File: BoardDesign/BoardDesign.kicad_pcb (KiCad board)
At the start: 2 copper layers, 77.5 x 67.3 mm, 10 parts

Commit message: Fixed Issue with R4 Trace
Had an accidental junction in the schematic.
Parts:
- renumbered 330 to R1, 10k to R5, Screen to U1, 74HC595 to U2
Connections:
- A1 pad 7: Net-(A1-Pad16) -> Net-(A1-Pad7)
- R1 pad 2: Net-(A1-Pad16) -> Net-(A1-Pad7)
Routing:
- net Net-(A1-Pad16): track 33.3 -> 57.5 mm, vias 0 -> 2
- net Net-(A1-Pad7): track 0.00 -> 6.68 mm

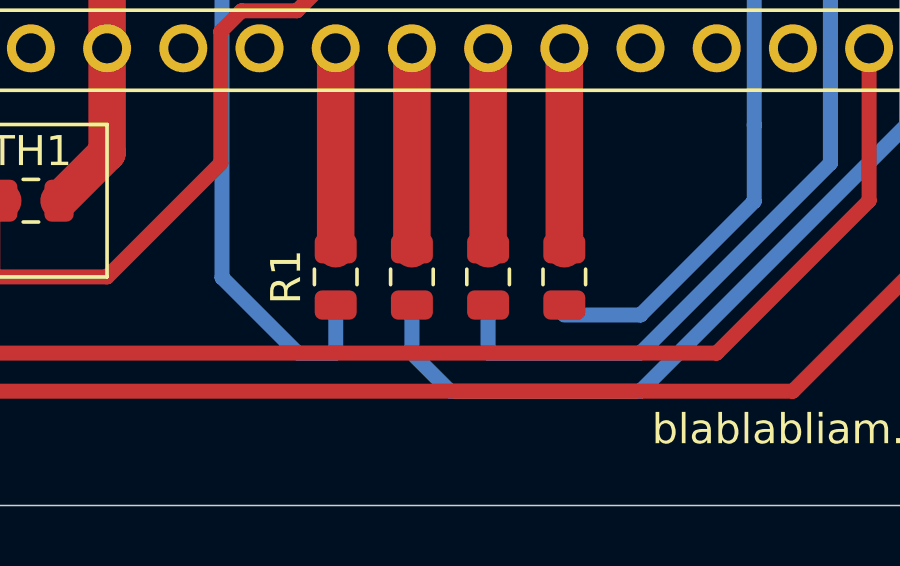
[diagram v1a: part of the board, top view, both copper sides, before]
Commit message: Fixed issue with 330 R trace on wrong side of board
The 330 ohm resistors have the traces on the wrong side of the board, so
that the resistors are not actually connected to anything. Fixed with 4
vias.
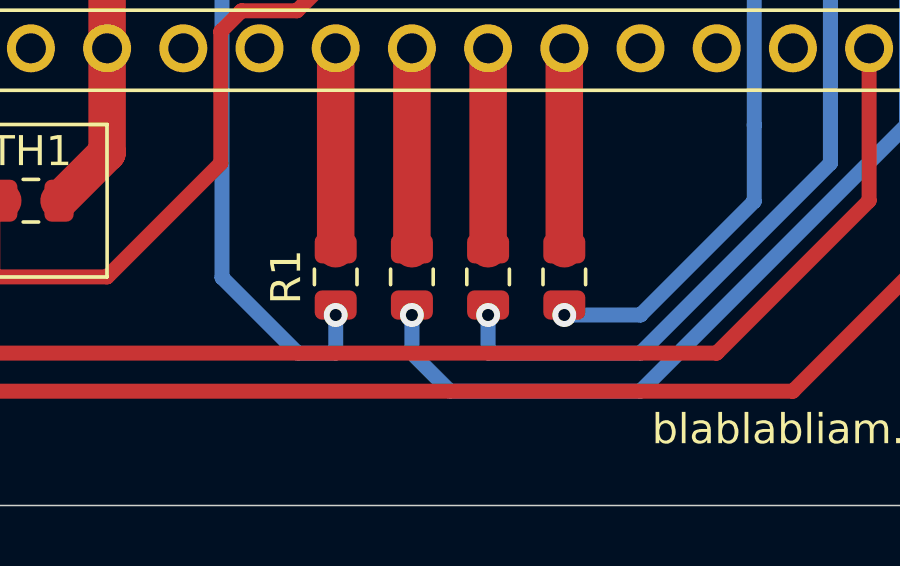
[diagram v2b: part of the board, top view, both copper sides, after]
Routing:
- net Net-(R4-Pad1): vias 0 -> 1
- net Net-(R3-Pad1): vias 0 -> 1
- net Net-(R2-Pad2): vias 0 -> 1
- net Net-(R1-Pad1): vias 0 -> 1

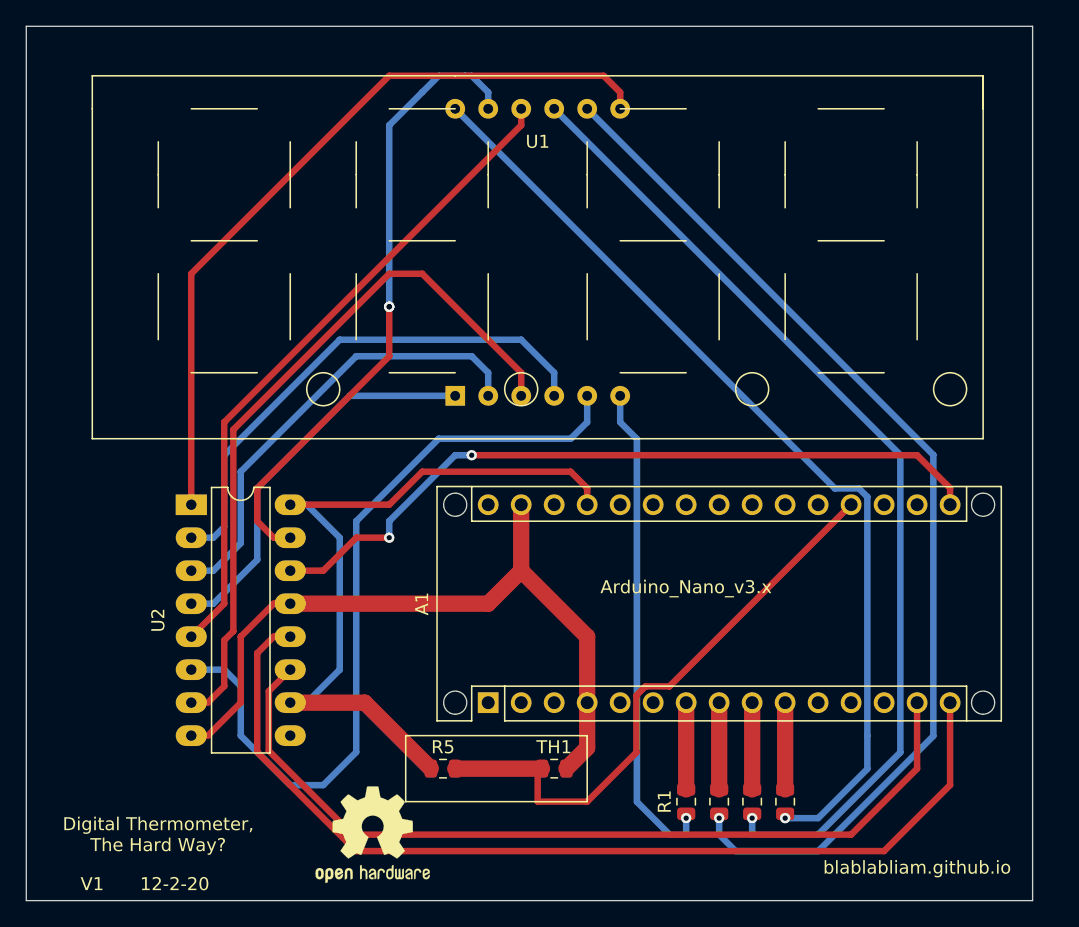
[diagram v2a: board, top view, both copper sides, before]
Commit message: Finished the V2 Design
Corrected the general issues with the board. Notably, fixed the
disconnected traces to the 330 Ohm resistors, swapped the positions of
the thermistor and loading resistor, added M2 screw holes and moved pin
13 to pin 10 for the coms to the shift register.
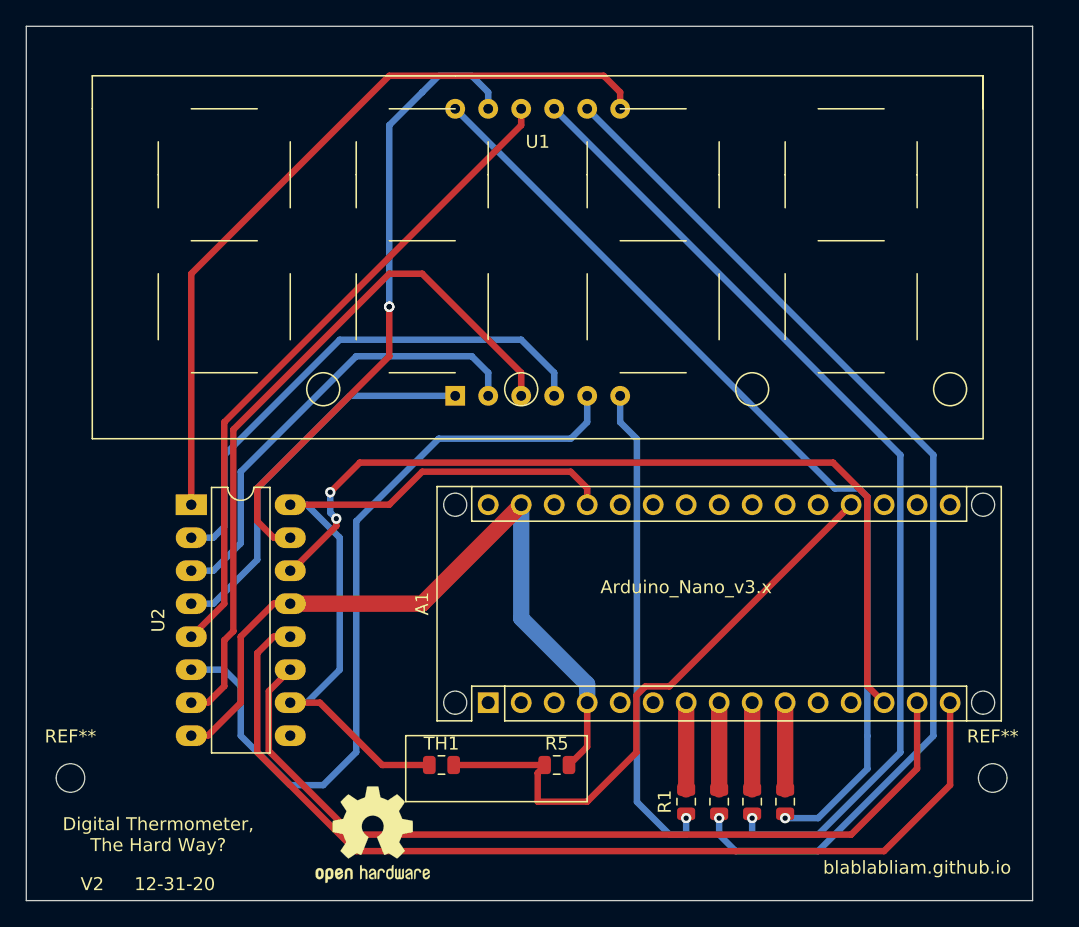
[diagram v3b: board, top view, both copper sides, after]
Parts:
- added REF**: MountingHole_2.2mm_M2, MountingHole:MountingHole_2.2mm_M2, F.Cu at (176.0, 82.0)
- added REF**: MountingHole_2.2mm_M2, MountingHole:MountingHole_2.2mm_M2, F.Cu at (105.0, 82.0)
- moved R5 8.76 mm to (142.4, 81.0)
- moved TH1 8.68 mm to (133.6, 81.0)
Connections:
- R5 pad 1: Net-(A1-Pad27) -> Net-(A1-Pad19)
- R5 pad 2: Net-(A1-Pad19) -> GND
- TH1 pad 1: Net-(A1-Pad19) -> Net-(A1-Pad27)
- TH1 pad 2: GND -> Net-(A1-Pad19)
- U2 pad 14: Net-(A1-Pad16) -> Net-(A1-Pad13)
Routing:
- net Net-(A1-Pad13): track 0.00 -> 67.5 mm, vias 0 -> 2
- net Net-(A1-Pad16): track 57.5 -> 0.00 mm, vias 2 -> 0
- net GND: track 56.7 -> 58.5 mm
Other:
- board text added: "12-31-20"
- board text added: "V2"
- board text removed: "12-2-20"
- board text removed: "V1"
